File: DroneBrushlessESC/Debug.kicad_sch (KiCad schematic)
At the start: 18 parts

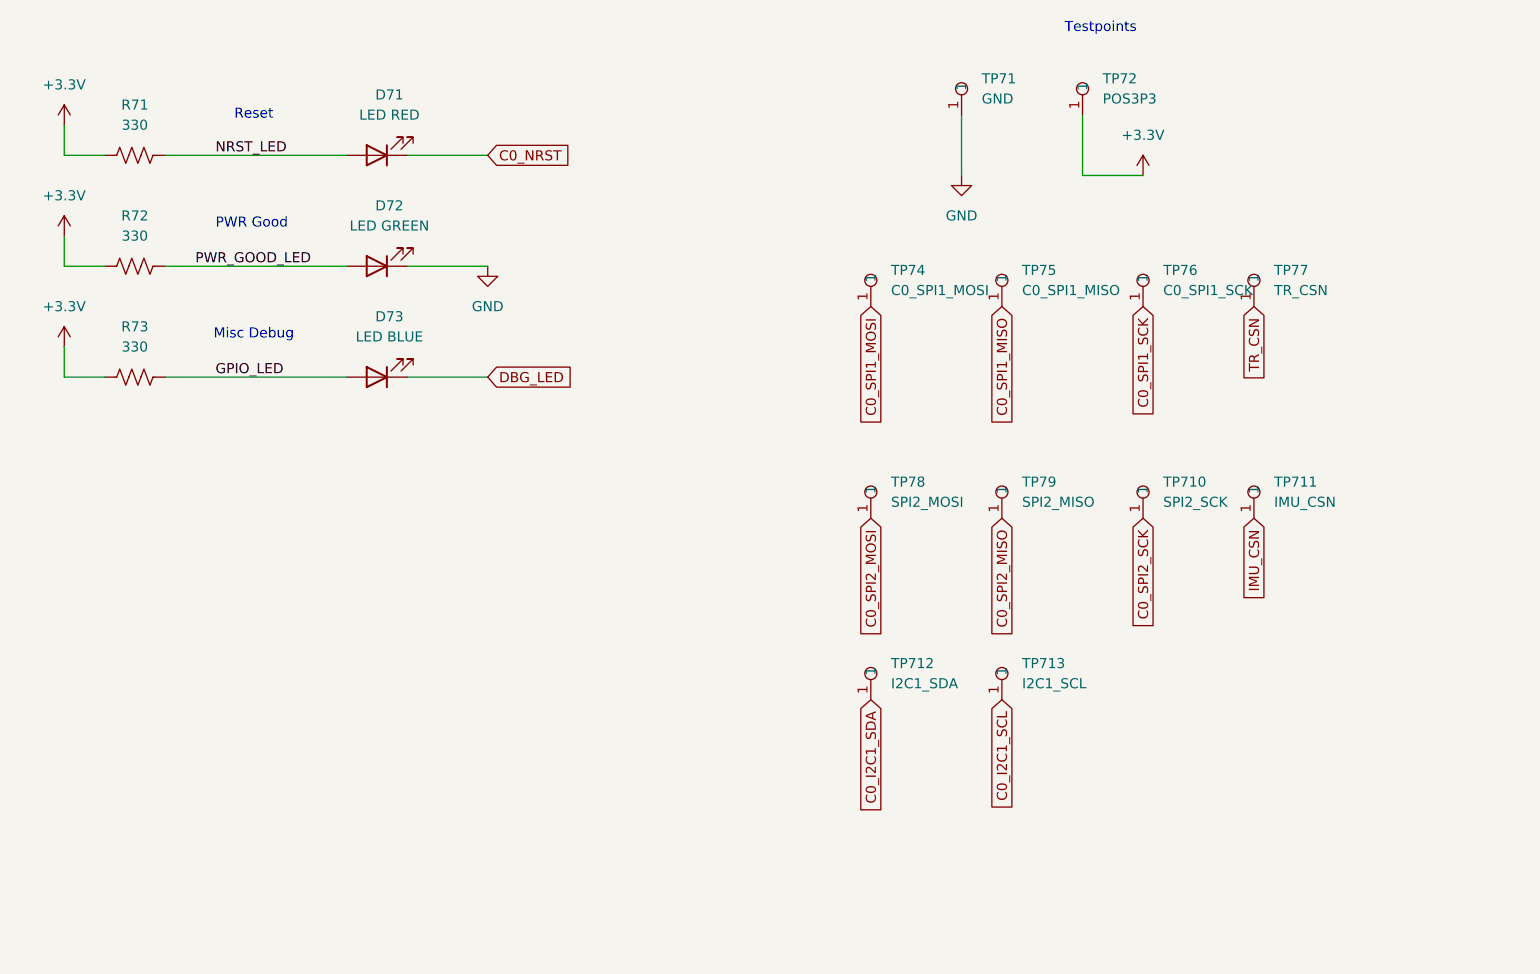
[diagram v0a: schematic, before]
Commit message: Completed schematic for brushless ESC and added needed components to main board.  The plan is to mount the ESCs on the main board using 2.54mm Vert Conn Headers
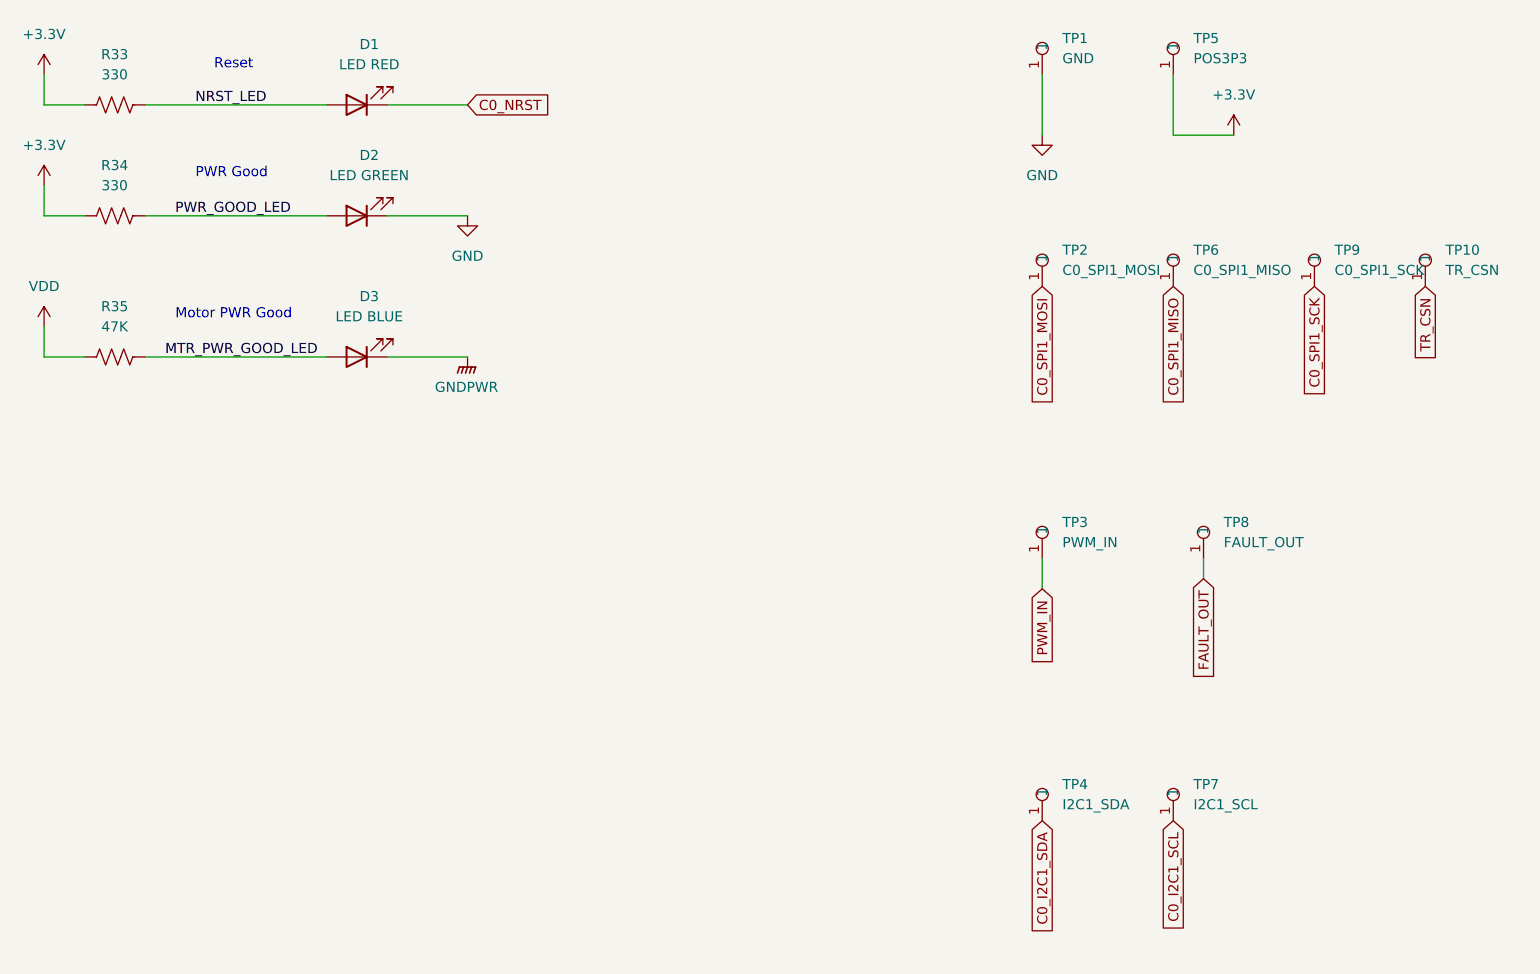
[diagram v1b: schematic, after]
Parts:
- removed R73: 330, Resistor_SMD:R_0402_1005Metric, symbol Device:R_US
- removed TP710: SPI2_SCK, Library:Testpoint 1.6mm x 0.8mm, symbol Global:Testpoint
- removed TP711: IMU_CSN, Library:Testpoint 1.6mm x 0.8mm, symbol Global:Testpoint
- removed TP78: SPI2_MOSI, Library:Testpoint 1.6mm x 0.8mm, symbol Global:Testpoint
- removed TP79: SPI2_MISO, Library:Testpoint 1.6mm x 0.8mm, symbol Global:Testpoint
- added R35: 47K, Resistor_SMD:R_0402_1005Metric, symbol Device:R_US
- added TP3: PWM_IN, Library:Testpoint 1.6mm x 0.8mm, symbol Global:Testpoint
- added TP8: FAULT_OUT, Library:Testpoint 1.6mm x 0.8mm, symbol Global:Testpoint
- renumbered D71 to D1, D72 to D2, D73 to D3, R71 to R33, R72 to R34, TP71 to TP1, TP77 to TP10, TP74 to TP2, TP712 to TP4, TP72 to TP5, TP75 to TP6, TP713 to TP7, TP76 to TP9
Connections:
- net DBG_LED renamed GNDPWR
- net GPIO_LED renamed MTR_PWR_GOOD_LED
- net MTR_PWR_GOOD_LED: now also R35.2
- new net FAULT_OUT: TP8.1
- new net PWM_IN: TP3.1
- new net VDD: R35.1
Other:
- note added: "Motor PWR Good"
- note removed: "Misc Debug"
- note removed: "Testpoints"
- title: Debug -> (none)
- moved on the sheet: D1, D2, D3, R33, R34, TP1, TP10, TP2, TP4, TP5, TP6, TP7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

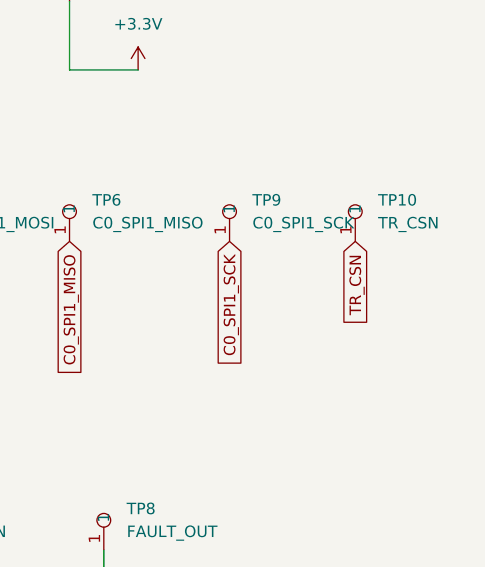
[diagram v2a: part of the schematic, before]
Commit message: Finished brushless driver layout
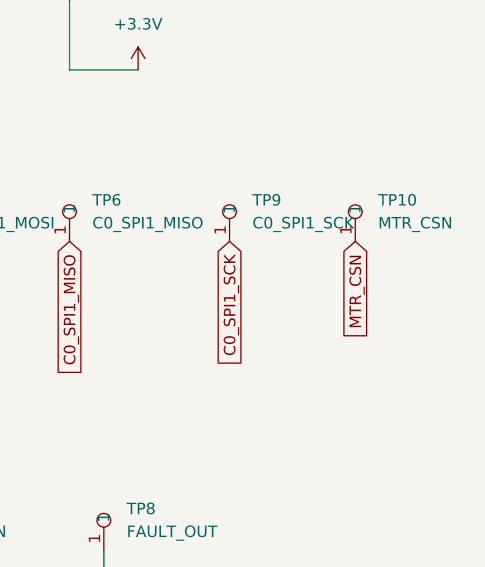
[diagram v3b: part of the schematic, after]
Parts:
- TP10: value TR_CSN -> MTR_CSN
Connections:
- net TR_CSN renamed MTR_CSN
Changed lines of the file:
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@@
 		)
 	)
-	(global_label "TR_CSN"
+	(global_label "MTR_CSN"
 		(shape input)
 		(at 200.66 54.61 270)
@@
 		)
 		(property "Intersheetrefs" "${INTERSHEET_REFS}"
-			(at 200.66 64.6104 90)
+			(at 200.66 66.0618 90)
 			(effects
 				(font
@@
 			)
 		)
-		(property "Value" "TR_CSN"
+		(property "Value" "MTR_CSN"
 			(at 203.2 52.5779 0)
 			(effects

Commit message: Finished Schematic for controller
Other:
- title: (none) -> Debug
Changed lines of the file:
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@@
 	(generator_version "9.0")
 	(paper "A4")
+	(title_block
+		(title "Debug")
+		(date "2026-02-23")
+		(rev "0-1")
+	)
 	(text "Reset"
 		(exclude_from_sim no)
